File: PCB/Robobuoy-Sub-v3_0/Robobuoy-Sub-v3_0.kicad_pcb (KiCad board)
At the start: 4 copper layers, 103 x 36 mm, 159 parts, among them J102 Display, J201 Prog, J203 ESC_BB, J301 CHRG/DATA, J302 ESC_SB, J303 ESC_BB, J304 ESC_PWR_SB, J305 ESC_PWR_BB, J306 LiPo S6, J401 Display, Q201 MMBT3904, Q202 MMBT5401, Q203 MMBT5401, Q204 MMBT3904, Q205 AO3400A, Q301 AO3400A, Q302 AO3401A, Q303 AO3401A, Q304 AO3400A, Q305 AO3400A, Q306 AON6407-MS, Q308 AON6407-MS, Q401 AO3400A, Q403 AO3400A, SW202 MODE, SW301 On/Off, U102 LSM303AGRTR, U201 LM1117S-3.3, U202 ESP32-WROOM-32E_(visible_peri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, U301 SN74LV1T34DBV, U302 SN74LV1T34DBV, U303 LMR16020PDDA, U304 TL082, U401 LP5907MFX-1.8, U403 ICM-20948

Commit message: Last cosmetic cleanupt
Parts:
- removed H201, H202, H203, H204: MountingHole, MountingHole:MountingHole_3.2mm_M3
- TP302: value Vcell -> VSAMP
- moved R318 14.3 mm to (55.9, 54.6)
- moved D303 12.6 mm to (56.9, 56.4)
- moved TP304 6.65 mm to (49.0, 34.4)
- moved C306 5.13 mm to (43.3, 51.2)
- moved C315 4.75 mm to (43.1, 43.6), turned to 90 degrees
- moved C314 4.60 mm to (54.7, 39.4), turned to -90 degrees
- moved TP301 4.57 mm to (69.8, 56.9)
- moved Q302 3.91 mm to (69.0, 60.0)
- moved R312 3.59 mm to (54.9, 43.0)
- moved R306 2.25 mm to (71.0, 61.6)
- moved TP302 1.58 mm to (73.8, 65.8)
- moved R214 1.44 mm to (74.6, 59.9)
- moved C307 1.42 mm to (74.6, 64.3)
- moved R304 1.42 mm to (74.6, 61.3)
- moved R307 1.42 mm to (74.6, 62.8)
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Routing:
- net Net-(J306--): track 34.5 -> 158.0 mm, vias 0 -> 20
- net GND: track 327.9 -> 418.9 mm, vias 135 -> 222
- net Vbatt: track 120.6 -> 134.7 mm, vias 1 -> 10
- net /Robobuoy-Sub-PSU-v3_0/COMM: track 39.0 -> 31.4 mm
- net Net-(J302-Pin_2): track 21.6 -> 16.8 mm
- net /CPU/ESC_SB: track 38.1 -> 41.2 mm
- net Net-(J302-Pin_1): track 11.6 -> 8.84 mm
- net /CPU/VSAMP: track 26.4 -> 28.9 mm
- net Net-(D204-DOUT): track 2.72 -> 4.53 mm
- net Net-(Q302-G): track 3.93 -> 5.73 mm
- net DR0: track 7.52 -> 9.01 mm
- net +3.3V: track 194.4 -> 195.5 mm
- net +5V: track 102.8 -> 103.9 mm
- net Net-(Q302-D): track 2.49 -> 1.48 mm
- net /CPU/SCL: track 31.1 -> 30.3 mm
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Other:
- outline, holes or cut-outs redrawn
- board text added: "+"
- board text added: "+5V"
- board text added: "-"
- board text added: "- + PWM"
- board text added: "3V3"
- board text added: "BUZZER"
- board text added: "D"
- board text added: "DATA"
- board text added: "GND"
- board text added: "L"
- board text added: "LED"
- board text added: "PWM + -"
- board text added: "ROBOBOY 3.0"
- board text added: "SCL"
- board text added: "SDA"
- board text added: "SW"

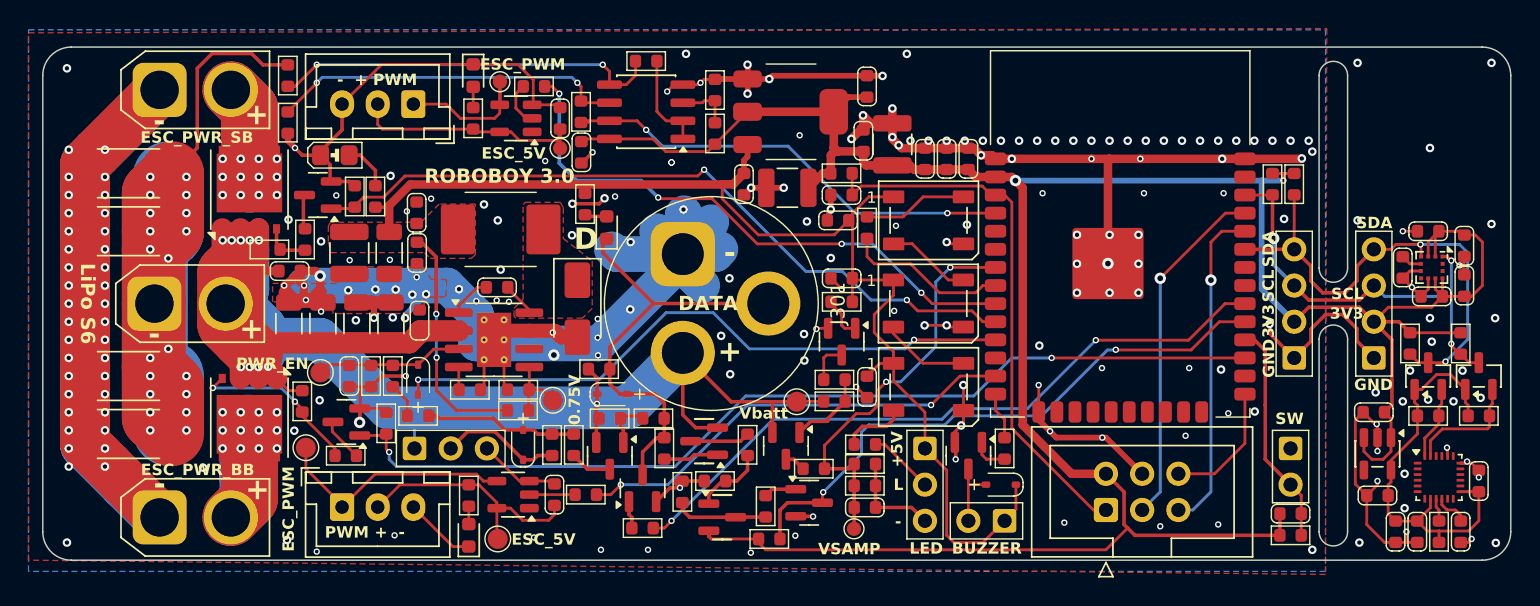
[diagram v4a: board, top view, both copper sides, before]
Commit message: Simulation added bms Little improvements BMS Resistor divider added on the gate of the mosfet (Limmeded to +/-20V could be 30V during charging)
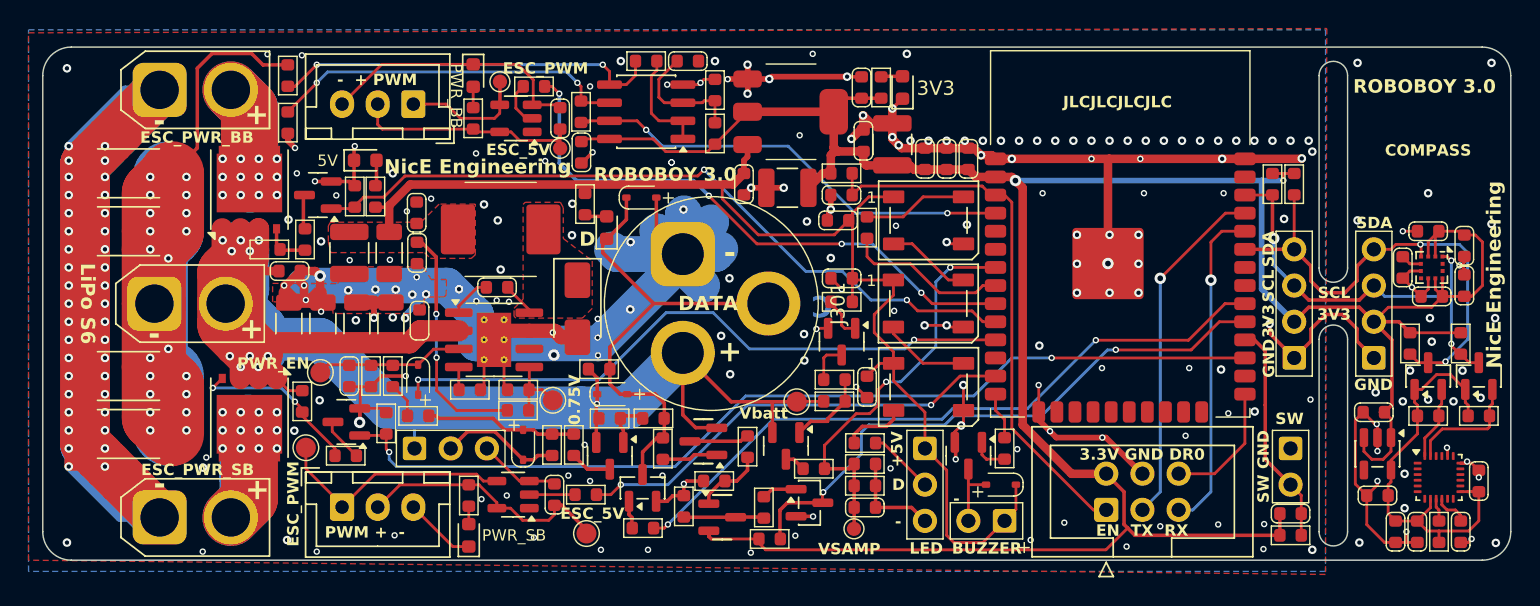
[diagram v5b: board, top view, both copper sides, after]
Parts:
- removed Q201, Q204: MMBT3904, Package_TO_SOT_SMD:SOT-23
- removed Q202, Q203: MMBT5401, PCM_JLCPCB:Q_SOT-23
- removed R202: 1k, A_Device:R_0603
- removed R203, R204, R205, R206, R207, R208: 10K, A_Device:R_0603
- added C316: 1n, A_Device:C_0603, F.Cu at (62.2, 33.0)
- added D205: GREEN, LED_SMD:LED_0603_1608Metric, F.Cu at (77.2, 34.8)
- added D309: 1N4148WS, A_Device:D_SOD-323_1.8x1.4x1.15, F.Cu at (58.9, 42.6)
- added PN101: ~, PCM_JLCPCB:Part_Num_JLCPCB, F.Cu at (92.3, 35.9)
- added Q102: MMBT3904, Package_TO_SOT_SMD:SOT-23, F.Cu at (70.7, 64.0)
- added Q117: MMBT3904, Package_TO_SOT_SMD:SOT-23, F.Cu at (59.0, 62.9)
- added Q307: MMBT5401, PCM_JLCPCB:Q_SOT-23, F.Cu at (63.3, 59.7)
- added Q309: MMBT5401, PCM_JLCPCB:Q_SOT-23, F.Cu at (64.6, 65.0)
- added R104: 2.2k, A_Device:R_0603, F.Cu at (75.7, 34.8)
- added R109: 10k, A_Device:R_0603, F.Cu at (60.4, 60.2)
- added R340: 1k, A_Device:R_0603, F.Cu at (59.0, 65.7)
- added R341: 10k, A_Device:R_0603, F.Cu at (66.3, 60.0)
- added R342: 10k, A_Device:R_0603, F.Cu at (64.0, 62.4)
- added R343: 10k, A_Device:R_0603, F.Cu at (61.9, 64.2)
- added R344: 10k, A_Device:R_0603, F.Cu at (67.5, 64.3)
- added R345: 10k, A_Device:R_0603, F.Cu at (67.9, 66.5)
- C317: value 4.7uF/10V -> 4.7uF/50V
- C404: value 10n -> 1n
- D304, D305: value PWR_ESC -> GREEN
- D308: value 3.3V -> GREEN; footprint A_Passive:LED_0805 -> LED_SMD:LED_0603_1608Metric
- J102: value Display -> I2C_OUT
- J302: value ESC_SB -> ESC_BB
- J303: value ESC_BB -> ESC_SB
- J304: value ESC_PWR_SB -> ESC_PWR_BB
- J305: value ESC_PWR_BB -> ESC_PWR_SB
- R105, R201, R210, R302, R305, R312, R325, R326, R329, R335, R336, R401, R402, R403, R404: value 10K -> 10k
- R303, R309, R310, R311, R313, R323, R324: value 100K -> 100k
- R308, R318: value 2K -> 2.2k
- R314, R317, R321: value 47K -> 47k
- R327, R328: value 18K -> 18k
- R331, R332: value 1.5K -> 1.5k
- R333, R334: value 4.6K -> 4.7k
- moved TP307 6.23 mm to (55.0, 66.1)
- moved D308 2.16 mm to (39.5, 39.9)
- moved C211 0.39 mm to (74.4, 34.8)
- moved R214 0.10 mm to (74.6, 59.8)
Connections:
- Q304 pad 1: /CPU/ESC_SB_PWR -> /CPU/ESC_BB_PWR
- Q305 pad 1: /CPU/ESC_BB_PWR -> /CPU/ESC_SB_PWR
- R315 pad 2: /CPU/ESC_BB -> /CPU/ESC_SB
- R316 pad 2: /CPU/ESC_SB -> /CPU/ESC_BB
- R323 pad 1: /CPU/ESC_SB_PWR -> /CPU/ESC_BB_PWR
- R324 pad 1: /CPU/ESC_BB_PWR -> /CPU/ESC_SB_PWR
- U202 pad 10: /CPU/ESC_SB_PWR -> /CPU/ESC_BB_PWR
- U202 pad 13: /CPU/ESC_BB -> /CPU/ESC_SB
- U202 pad 27: /CPU/ESC_BB_PWR -> /CPU/ESC_SB_PWR
- U202 pad 29: RX_SUB -> /CPU/RX_SUB
- U202 pad 30: TX_SUB -> /CPU/TX_SUB
- U202 pad 9: /CPU/ESC_SB -> /CPU/ESC_BB
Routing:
- net TX_SUB: track 48.0 -> 0.00 mm, vias 2 -> 0
- net /CPU/TX_SUB: track 0.00 -> 48.0 mm, vias 0 -> 2
- net RX_SUB: track 41.4 -> 0.00 mm, vias 2 -> 0
- net /CPU/RX_SUB: track 0.00 -> 41.4 mm, vias 0 -> 2
- net GND: track 418.9 -> 436.9 mm, vias 222 -> 247
- net /CPU/ESC_SB_PWR: track 52.2 -> 67.2 mm
- net /CPU/ESC_BB_PWR: track 67.2 -> 52.2 mm
- net /CPU/ESC_SB: track 41.2 -> 31.4 mm, vias 4 -> 2
- net /CPU/ESC_BB: track 31.4 -> 41.1 mm, vias 2 -> 4
- net Vbatt: track 134.7 -> 143.5 mm, vias 10 -> 11
- net Net-(Q203-C): track 6.58 -> 0.00 mm
- net Net-(Q309-C): track 0.00 -> 5.75 mm
- net Net-(Q309-B): track 0.00 -> 5.10 mm
- net Net-(Q203-B): track 5.10 -> 0.00 mm
- net Net-(U304A-+): track 3.86 -> 8.78 mm
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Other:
- board text added: "+ GND ACCU"
- board text added: "+ GND ESC BB"
- board text added: "3.3V GND DR0"
- board text added: "5V BUZZER"
- board text added: "5V D (led) GND"
- board text added: "C"
- board text added: "COMPASS"
- board text added: "CPU / PWR CONTROLLER"
- board text added: "DR0 GND 3.3V"
- board text added: "EN TX RX"
- board text added: "ESC SB + GND"
- board text added: "GND SW"
- board text added: "NicE Engineering"
- board text added: "NicE Engineering ROBOBOY 3.0"
- board text added: "RX TX EN"
- board text added: "SDA SCL 3.3V GND"
- board text added: "SW GND"
- board text added: "VBATT"
- board text added: "VBATT on C off GND"
- board text removed: "L"

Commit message: PCB adjustmend Sub V3.0
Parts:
- moved C207 0.13 mm to (66.1, 41.5)
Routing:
- net +5V: track 103.9 -> 102.8 mm
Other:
- board text added: "5V"
- board text removed: "+5V"
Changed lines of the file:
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@@
 		)
 		(property "Text" "3V3"
-			(at -0.0508 2.3368 0)
+			(at -0.0508 3.2258 0)
 			(unlocked yes)
 			(layer "F.SilkS")
@@
 		(tags "RC Connector XT60")
 		(property "Reference" "J301"
-			(at 0 -8.89 270)
+			(at 0 3.553259 180)
 			(layer "F.SilkS")
 			(effects
@@
 	(footprint "A_Device:C_0603"
 		(layer "F.Cu")
-		(at 66.096 41.618 -90)
+		(at 66.096 41.491 -90)
 		(descr "Capacitor, 1608metric")
 		(property "Reference" "C207"
@@
 	)
 	(gr_text "NicE Engineering"
-		(at 119.309 47.968 90)
+		(at 119.309 46.825 90)
 		(layer "F.SilkS")
 		(effects
@@
 		)
 	)
+	(gr_text "NicE Engineering"
+		(at 17.455 50 270)
+		(layer "F.SilkS")
+		(effects
+			(font
+				(size 1 1)
+				(thickness 0.2)
+				(bold yes)
+			)
+			(justify bottom)
+		)
+	)
 	(gr_text "SCL"
 		(at 107.498 49.238 0)
@@
 	)
 	(gr_text "COMPASS"
-		(at 114.102 39.713 0)
+		(at 114.102 40.348 0)
 		(layer "F.SilkS")
 		(effects
@@
 	)
 	(gr_text "DATA"
-		(at 63.580293 49.991436 0)
+		(at 64.699 50 270)
 		(layer "F.SilkS")
 		(effects
@@
 	)
 	(gr_text "D"
-		(at 54.539 46.063 0)
+		(at 57.206 45.174 0)
 		(layer "F.SilkS")
 		(effects
@@
 	)
 	(gr_text "ROBOBOY 3.0"
-		(at 113.848 34.76 0)
+		(at 113.848 37.3 0)
 		(layer "F.SilkS")
 		(effects
@@
 		)
 	)
-	(gr_text "+5V"
-		(at 76.8402 60.2108 90)
+	(gr_text "5V"
+		(at 76.704046 60.211668 0)
 		(layer "F.SilkS")
 		(effects
@@
 	)
 	(gr_text "CPU / PWR CONTROLLER"
-		(at 96.83 51.143 0)
+		(at 88.067 50 0)
 		(layer "B.SilkS")
 		(effects
@@
 				(bold yes)
 			)
-			(justify left bottom mirror)
+			(justify mirror)
 		)
 	)
@@
 	)
 	(segment
-		(start 64.572 41.63)
-		(end 65.334002 41.63)
-		(width 0.6)
-		(layer "F.Cu")
-		(net 1)
-	)
-	(segment
 		(start 85.18 62.7)
 		(end 85.18 64.444)
@@
 	)
 	(segment
+		(start 65.322 40.741)
+		(end 66.096 40.741)
+		(width 0.6)
+		(layer "F.Cu")
+		(net 1)
+	)
+	(segment
 		(start 64.5586 41.6434)
 		(end 42.6772 41.6434)
@@
 	)
 	(segment
-		(start 65.345 41.619002)
-		(end 66.096002 40.868)
-		(width 0.2)
-		(layer "F.Cu")
-		(net 1)
-	)
-	(segment
 		(start 44.5314 56.096)
 		(end 44.5314 53.7846)
@@
 	)
 	(segment
+		(start 64.572 41.63)
+		(end 64.572 41.491)
+		(width 0.6)
+		(layer "F.Cu")
+		(net 1)
+	)
+	(segment
 		(start 43.1598 45.694)
 		(end 43.4766 45.694)
@@
 	)
 	(segment
-		(start 82.86 66.764)
-		(end 84.384 65.24)
-		(width 0.2)
+		(start 66.096 39.9416)
+		(end 66.096 40.741)
+		(width 0.4)
 		(layer "F.Cu")
 		(net 1)
 	)
 	(segment
-		(start 66.096002 40.868)
-		(end 66.096 40.867998)
-		(width 0.4)
+		(start 64.572 41.491)
+		(end 65.322 40.741)
+		(width 0.6)
+		(layer "F.Cu")
+		(net 1)
+	)
+	(segment
+		(start 82.86 66.764)
+		(end 84.384 65.24)
+		(width 0.2)
 		(layer "F.Cu")
 		(net 1)
@@
 	)
 	(segment
-		(start 66.096 40.867998)
-		(end 66.096 39.9416)
-		(width 0.4)
-		(layer "F.Cu")
-		(net 1)
-	)
-	(segment
-		(start 65.334002 41.63)
-		(end 66.096002 40.868)
-		(width 0.6)
-		(layer "F.Cu")
-		(net 1)
-	)
-	(segment
 		(start 85.18 64.444)
 		(end 84.384 65.24)
@@
 	)
 	(segment
+		(start 66.096 42.368)
+		(end 66.592 41.872)
+		(width 0.4)
+		(layer "F.Cu")
+		(net 3)
+	)
+	(segment
 		(start 19.866 40.234)
 		(end 20.699 39.401)
@@
 	)
 	(segment
-		(start 66.604 41.872)
-		(end 66.592 41.872)
-		(width 0.4)
-		(layer "F.Cu")
-		(net 3)
-	)
-	(segment
 		(start 19.866 53.048)
 		(end 19.866 52.286)
@@
 	)
 	(segment
-		(start 66.592 41.872)
-		(end 66.096 42.368)
-		(width 0.4)
-		(layer "F.Cu")
-		(net 3)
-	)
-	(segment
 		(start 66.35 34.238)
 		(end 67.874 34.238)
@@
 	)
 	(segment
+		(start 66.592 41.872)
+		(end 66.858 41.872)
+		(width 0.4)
+		(layer "F.Cu")
+		(net 3)
+	)
+	(segment
 		(start 110.546 58.502005)
 		(end 110.491844 58.447849)
@@
 	)
 	(segment
-		(start 67.669 41.872)
-		(end 66.604 41.872)
-		(width 0.4)
-		(layer "F.Cu")
-		(net 3)
-	)
-	(segment
 		(start 52.8282 51.9059)
 		(end 53.2779 52.3556)
@@
 	)
 	(segment
+		(start 66.858 41.872)
+		(end 67.669 41.872)
+		(width 0.4)
+		(layer "F.Cu")
+		(net 3)
+	)
+	(segment
 		(start 34.4984 49.795)
 		(end 35.7808 49.795)
@@
 	)
 	(via
-		(at 66.604 41.872)
+		(at 66.858 41.872)
 		(size 0.6)
 		(drill 0.3)

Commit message: Heel veel AI veranderingen.
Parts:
- added C501: 100u/10V, Capacitor_SMD:C_1210_3225Metric, F.Cu at (113.9, 42.6)
- added D310: 1N4148WS, A_Device:D_SOD-323_1.8x1.4x1.15, F.Cu at (60.9, 40.3)
- added R346: 100, A_Device:R_0603, F.Cu at (57.3, 40.1)
- added R501: 10k, A_Device:R_0603, F.Cu at (119.1, 62.4)
- moved C311 1.96 mm to (50.7, 48.9)
- moved R320 0.13 mm to (46.8, 63.3)
- moved R316 0.13 mm to (51.4, 34.6)
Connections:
- C314 pad 1: +3.3V -> +5V
- R333 pad 2: /CPU/Imon -> Net-(R333-Pad2)
- U304 pad 7: /CPU/Imon -> Net-(R333-Pad2)
- U304 pad 8: +3.3V -> +5V
- U403 pad 22: unconnected-(U403-~{CS}-Pad22) -> Net-(U403-~{CS})
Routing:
- net +5V: track 102.8 -> 119.7 mm
- net GND: track 436.9 -> 422.9 mm, vias 247 -> 259
- net Net-(U403-~{CS}): track 0.00 -> 7.49 mm
- net Net-(R333-Pad2): track 0.00 -> 7.08 mm
- net Vbatt: track 143.5 -> 138.7 mm
- net +3.3V: track 196.4 -> 191.7 mm
- net /CPU/Imon: track 31.8 -> 28.3 mm
- net Net-(U303-BOOT): track 2.94 -> 5.39 mm, vias 0 -> 2
- net +1.8V: track 29.5 -> 30.9 mm
- net /CPU/RX_SUB: track 41.4 -> 40.5 mm
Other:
- board text added: "NicE Engineering ROBOBOY SUB 3.0"
- board text added: "ON OFF"
- board text added: "ROBOBOY SUB 3.0"
- board text added: "ROBOBOY_SUB"
- board text added: "VBATT C GND"
- board text removed: "NicE Engineering ROBOBOY 3.0"
- board text removed: "VBATT on C off GND"

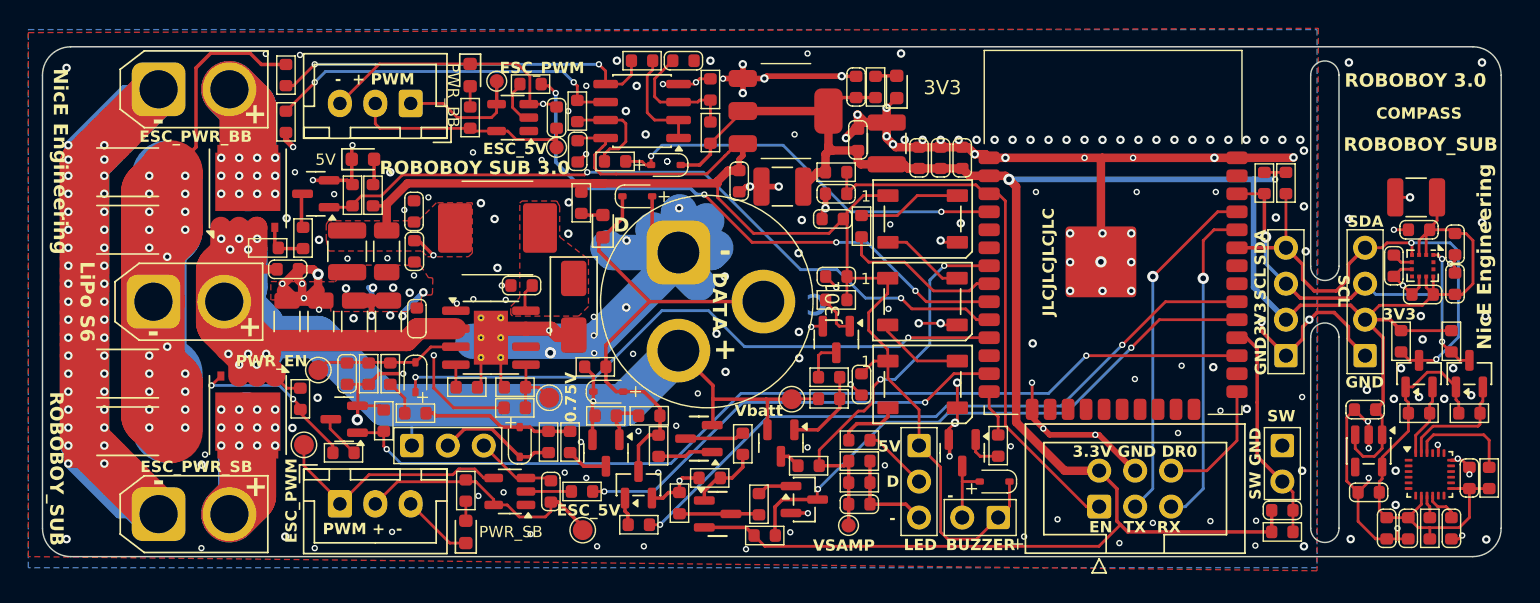
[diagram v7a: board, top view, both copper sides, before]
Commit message: BMS asd SUB orderd at JLCPCB
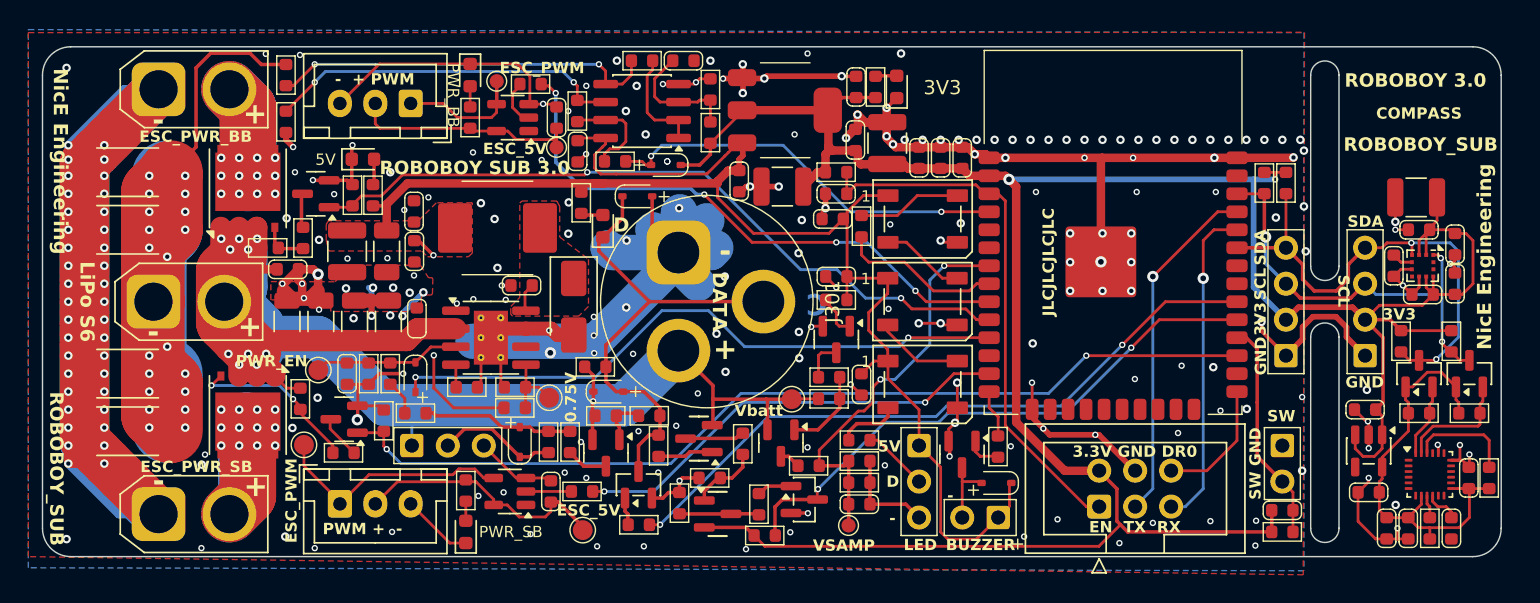
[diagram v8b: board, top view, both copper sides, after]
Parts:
- PN101: value ~ -> Partnumber JLCPCB
- moved C102 0.18 mm to (74.3, 38.6)
- moved D201 0.16 mm to (84.3, 62.8)
- moved Q205 0.11 mm to (81.8, 60.8)
- moved U201 0.08 mm to (69.3, 36.5)
- moved R209 0.07 mm to (84.4, 60.2)
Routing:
- net GND: track 422.9 -> 453.6 mm, vias 259 -> 242
- net (no net): vias 2 -> 0
